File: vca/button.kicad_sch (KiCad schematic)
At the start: 4 parts, among them SW2 SW_Push

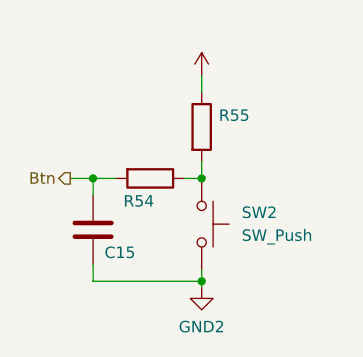
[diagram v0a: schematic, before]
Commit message: fixing drc issues
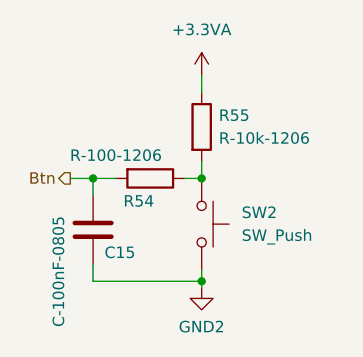
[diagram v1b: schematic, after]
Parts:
- C15: value (none) -> C-100nF-0805; footprint (none) -> Capacitor_SMD:C_0805_2012Metric_Pad1.18x1.45mm_HandSolder
- R54: value (none) -> R-100-1206; footprint (none) -> Resistor_SMD:R_1206_3216Metric_Pad1.30x1.75mm_HandSolder
- R55: value (none) -> R-10k-1206; footprint (none) -> Resistor_SMD:R_1206_3216Metric_Pad1.30x1.75mm_HandSolder
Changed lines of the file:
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@@
       (effects (font (size 1.27 1.27)) (justify left))
     )
-    (property "Value" "" (id 1) (at 110.49 73.0249 0)
+    (property "Value" "R-10k-1206" (id 1) (at 110.49 73.0249 0)
       (effects (font (size 1.27 1.27)) (justify left))
     )
-    (property "Footprint" "" (id 2) (at 106.807 71.755 90)
+    (property "Footprint" "Resistor_SMD:R_1206_3216Metric_Pad1.30x1.75mm_HandSolder" (id 2) (at 106.807 71.755 90)
       (effects (font (size 1.27 1.27)) hide)
     )
@@
       (effects (font (size 1.27 1.27)) hide)
     )
-    (property "Value" "" (id 1) (at 108.585 60.96 0))
+    (property "Value" "+3.3VA" (id 1) (at 108.585 60.96 0))
     (property "Footprint" "" (id 2) (at 108.585 66.04 0)
       (effects (font (size 1.27 1.27)) hide)
@@
       (effects (font (size 1.27 1.27)) (justify left))
     )
-    (property "Value" "" (id 1) (at 92.71 93.98 90)
+    (property "Value" "C-100nF-0805" (id 1) (at 92.71 93.98 90)
       (effects (font (size 1.27 1.27)) (justify left))
     )
-    (property "Footprint" "" (id 2) (at 97.4852 86.995 0)
+    (property "Footprint" "Capacitor_SMD:C_0805_2012Metric_Pad1.18x1.45mm_HandSolder" (id 2) (at 97.4852 86.995 0)
       (effects (font (size 1.27 1.27)) hide)
     )
@@
     (in_bom yes) (on_board yes)
     (property "Reference" "R54" (id 0) (at 101.6 80.01 90))
-    (property "Value" "" (id 1) (at 99.06 74.93 90))
-    (property "Footprint" "" (id 2) (at 102.87 75.692 90)
+    (property "Value" "R-100-1206" (id 1) (at 99.06 74.93 90))
+    (property "Footprint" "Resistor_SMD:R_1206_3216Metric_Pad1.30x1.75mm_HandSolder" (id 2) (at 102.87 75.692 90)
       (effects (font (size 1.27 1.27)) hide)
     )
